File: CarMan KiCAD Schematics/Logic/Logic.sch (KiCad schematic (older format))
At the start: 48 parts, among them J1 MC_CAN, J3 IMU, J4 RTC, J5.1 Conn_01x06, J5.2 Conn_01x06, J6 You're Welcome -Ethan, J7 GLV BOB, J8 PIC program, U1 MCP9700AT-HTT, U10 TLP293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

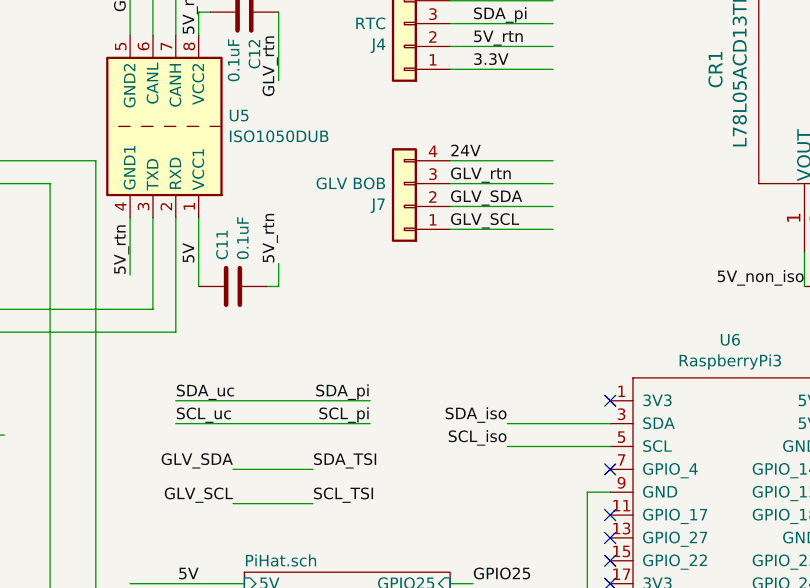
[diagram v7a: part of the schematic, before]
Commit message: Logic PCB updates, Fixed I2C and ground connections in Logic
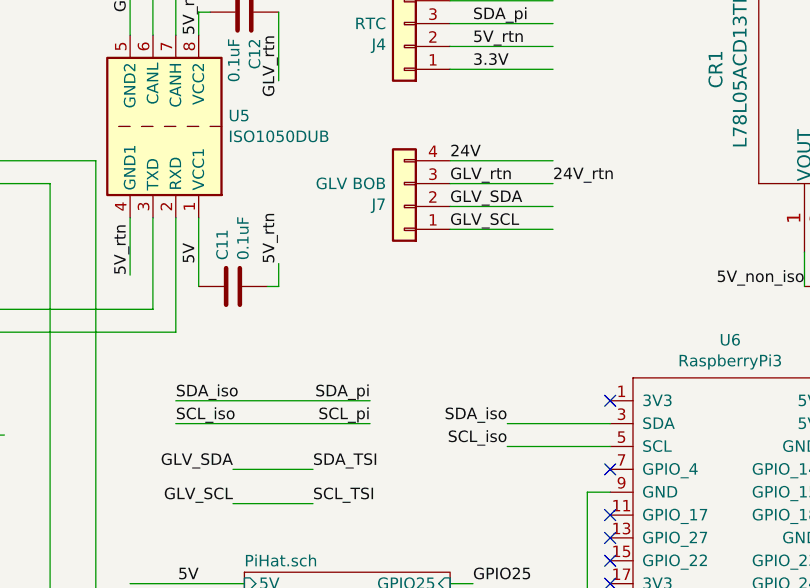
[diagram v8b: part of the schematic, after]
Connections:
- net labels removed: SCL_uc, SDA_uc
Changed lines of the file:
@@
 Text Label 8450 3250 2    50   ~ 0
 SCL_pi
-Text Label 7600 3150 0    50   ~ 0
-SDA_uc
-Text Label 7600 3250 0    50   ~ 0
-SCL_uc
 $Comp
 L Device:R R8
@@
 Text Label 10550 3850 0    50   ~ 0
 Safety_Loop_iso
+Text Label 7600 3150 0    50   ~ 0
+SDA_iso
+Text Label 7600 3250 0    50   ~ 0
+SCL_iso
+Text Label 9250 2200 0    50   ~ 0
+24V_rtn
 $EndSCHEMATC
